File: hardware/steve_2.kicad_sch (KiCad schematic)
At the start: 22 parts, among them J2 Micro_SD_Card_Det2, J3 TE_1-2834015-4_Buchanan_WireM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, U2 TI_TPS51386RJNR_Regulator_Buc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

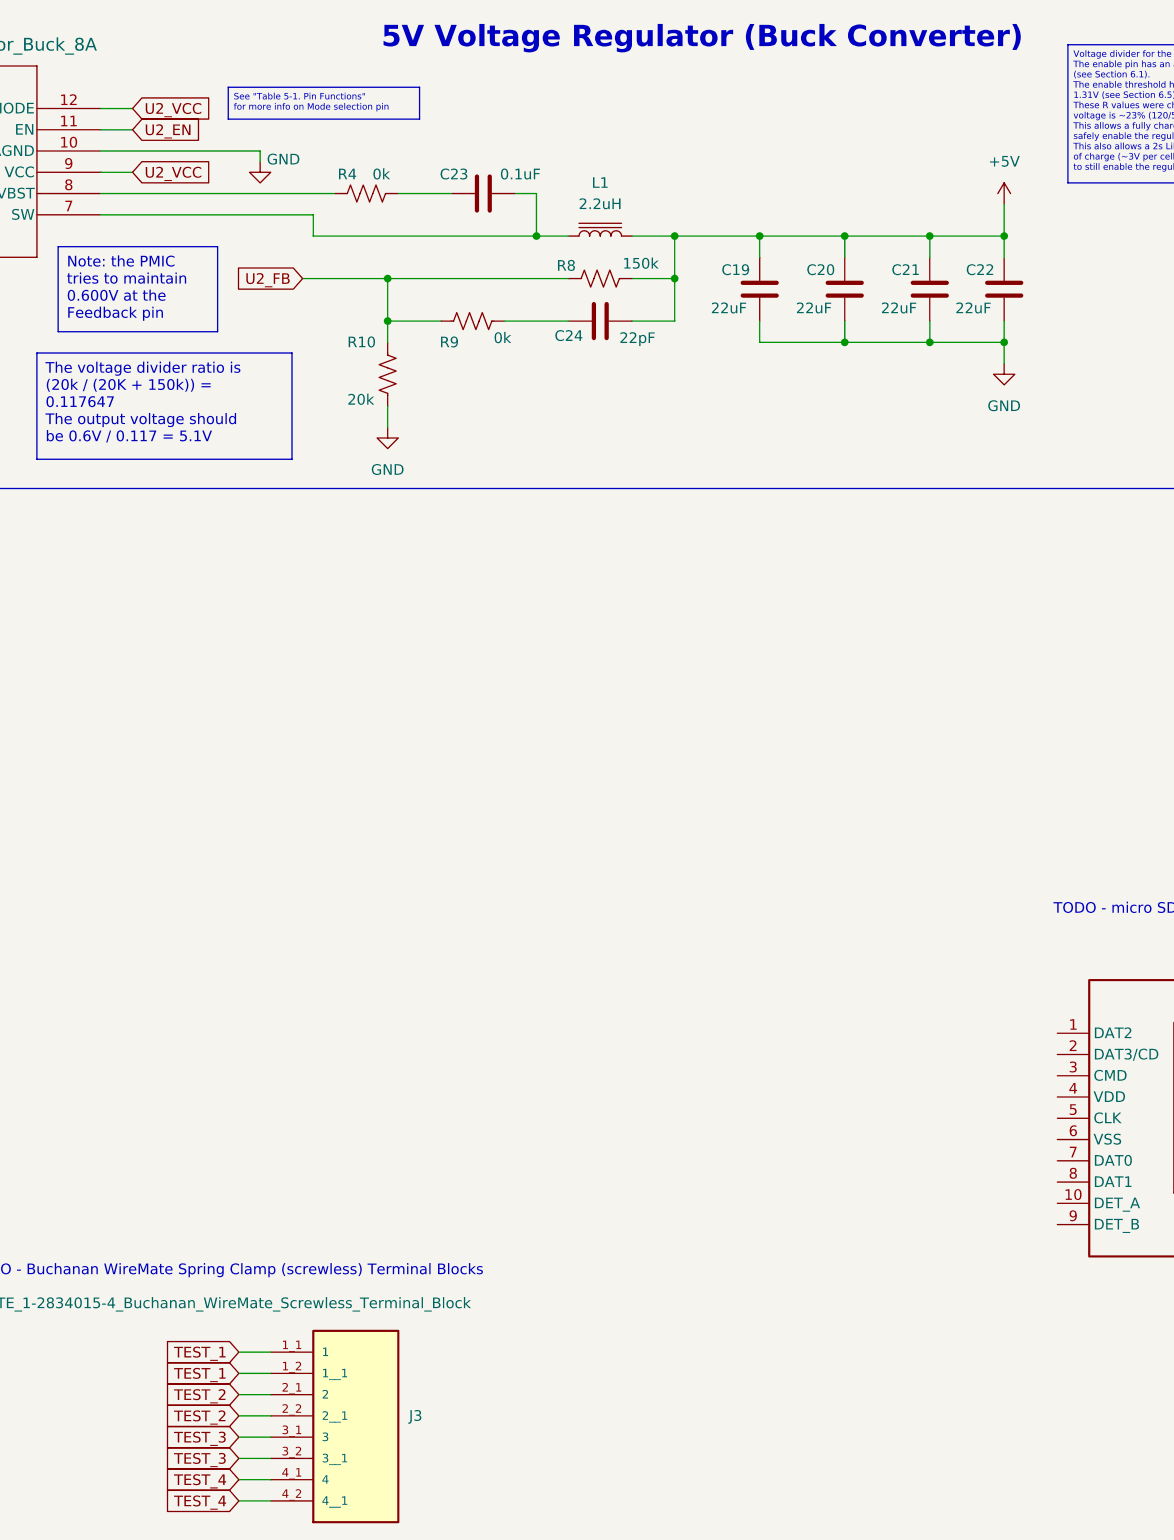
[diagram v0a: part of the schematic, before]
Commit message: import BMP388, add BMP388 to pcb and sch
Import BMP388 symbol and footprint to project imports dir. Add BMP388 symbol to schematic and footprint to pcb.
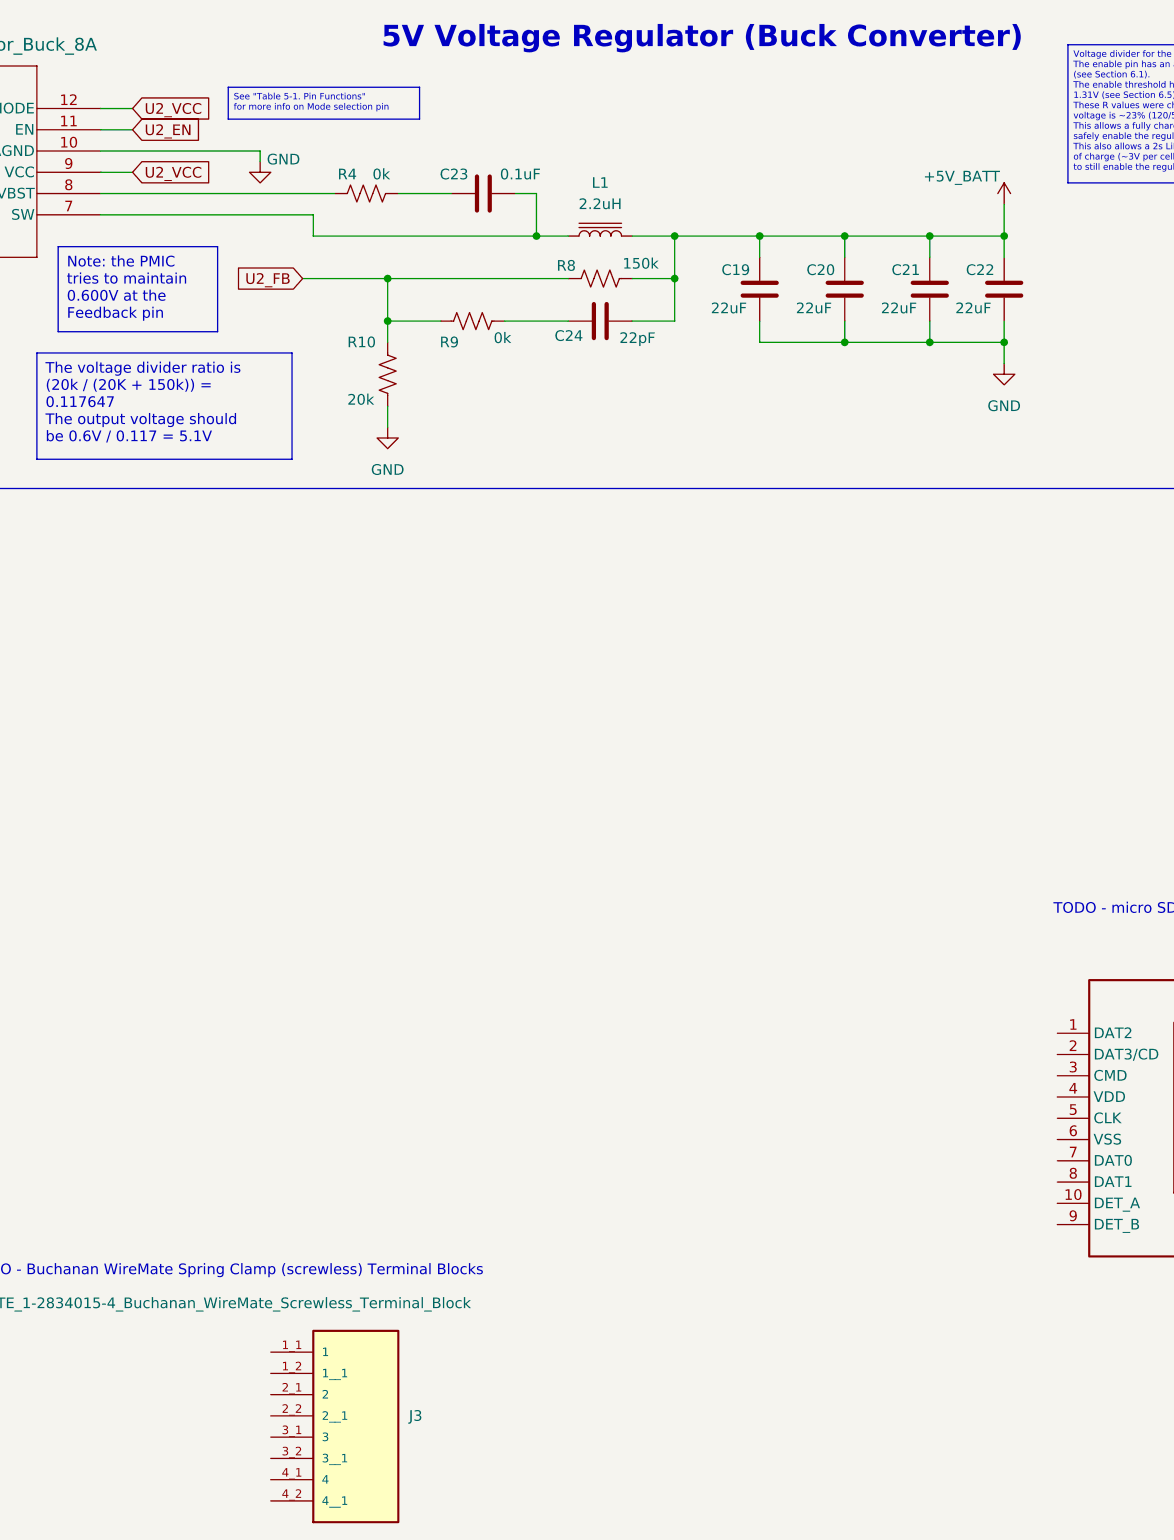
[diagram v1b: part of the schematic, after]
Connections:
- net +5V renamed +5V_BATT
- net TEST_1: no longer names the net of J3.1_1 (1)
- net TEST_1: no longer J3.1_2 (1__1)
- net TEST_2: no longer names the net of J3.2_1 (2)
- net TEST_2: no longer J3.2_2 (2__1)
- net TEST_3: no longer names the net of J3.3_1 (3)
- net TEST_3: no longer J3.3_2 (3__1)
- net TEST_4: no longer names the net of J3.4_1 (4)
- net TEST_4: no longer J3.4_2 (4__1)

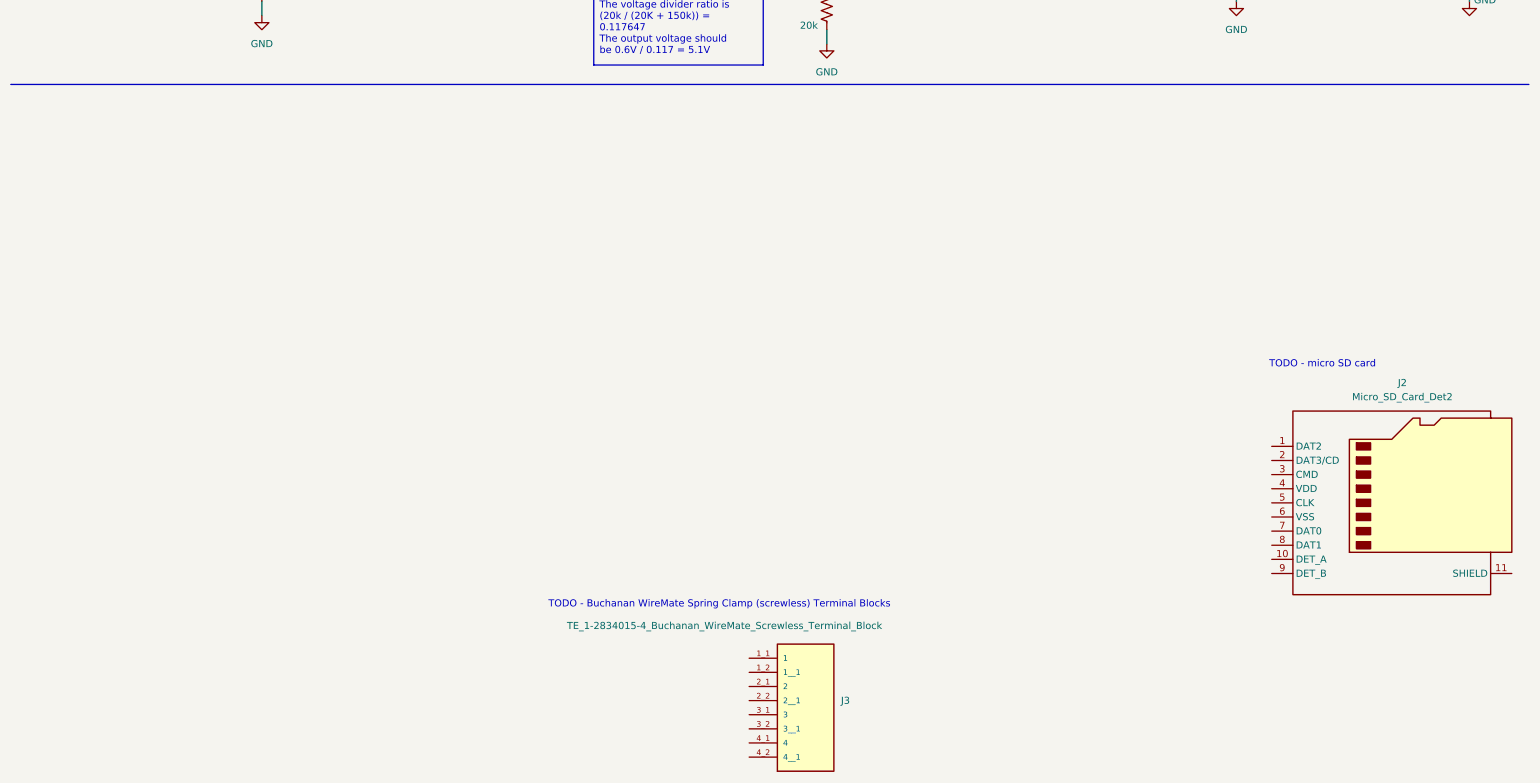
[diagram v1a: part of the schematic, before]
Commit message: Finished sensor, flash, and SD card in schematic; Updated README for remaining items
Finished BMI270 and BMP390, Flash storage, and  microSD card in schematic; Updated README for remaining items
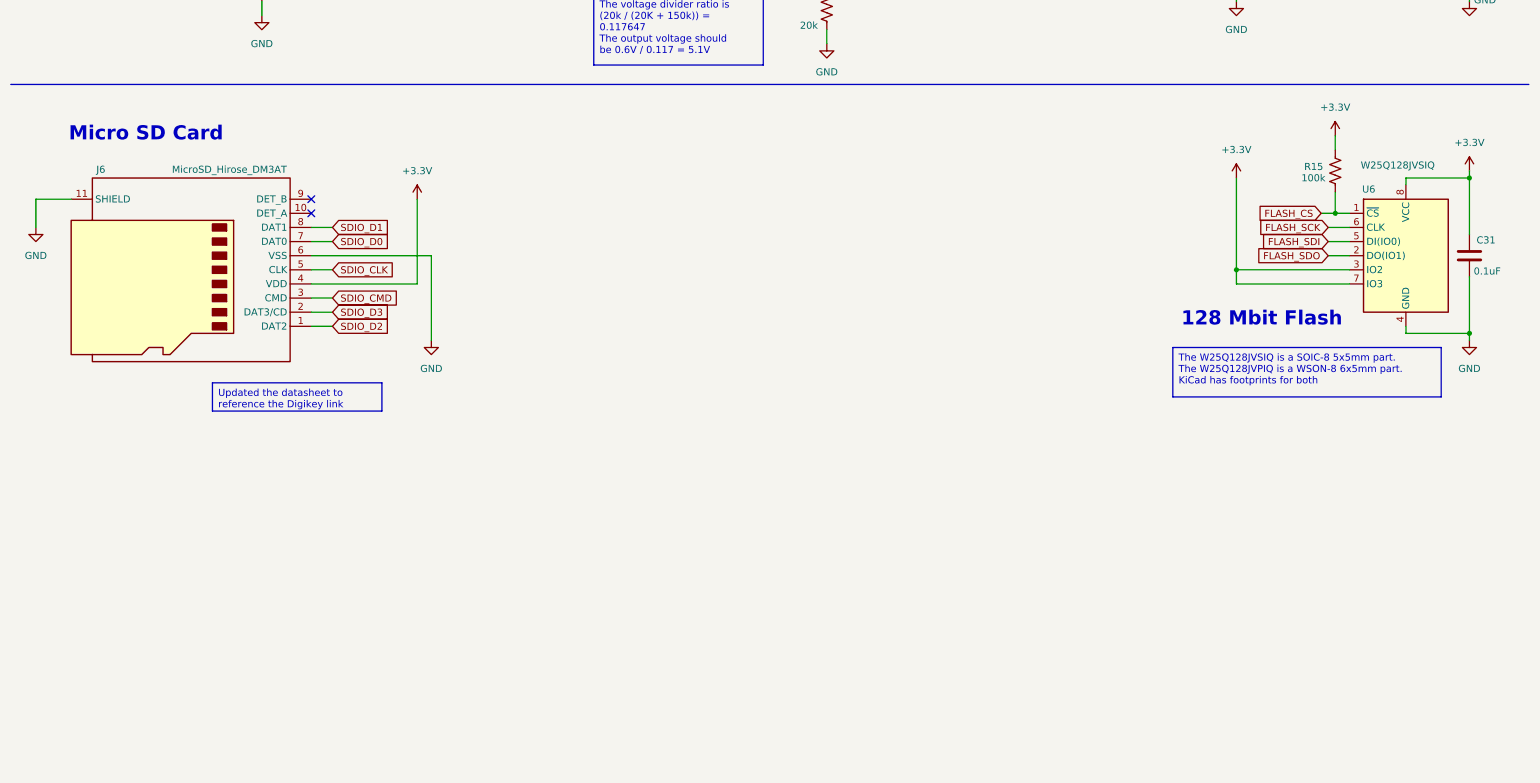
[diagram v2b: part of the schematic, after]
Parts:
- removed J2: Micro_SD_Card_Det2, Connector_Card:microSD_HC_Molex_104031-0811, symbol Connector:Micro_SD_Card_Det2
- removed J3: TE_1-2834015-4_Buchanan_WireMate_Screwless_Termin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, Imported_Footprints:TE_1-2834015-4_Buchanan_WireMate_Screwless_Terminal_Block, symbol Imported_Symbols:TE_1-2834015-4_Buchanan_WireMate_Screwless_Terminal_Block
- added C31: 0.1uF, Capacitor_SMD:C_0603_1608Metric, symbol Device:C
- added J6: MicroSD_Hirose_DM3AT, Connector_Card:microSD_HC_Hirose_DM3AT-SF-PEJM5, symbol Connector:Micro_SD_Card_Det_Hirose_DM3AT
- added R15: 100k, Resistor_SMD:R_0603_1608Metric, symbol Device:R_US
- added U6: W25Q128JVSIQ, Package_SO:SOIC-8_5.23x5.23mm_P1.27mm, symbol Memory_Flash:W25Q128JVS
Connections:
- net GND: now also C31.2, J6.11 (SHIELD), J6.6 (VSS), U6.4 (GND)
- new net +3.3V: C31.1, J6.4 (VDD), R15.1, U6.3 (IO2), U6.7 (IO3), U6.8 (VCC)
- new net FLASH_CS: R15.2, U6.1 (~{CS})
- new net FLASH_SCK: U6.6 (CLK)
- new net FLASH_SDI: U6.5 (DI(IO0))
- new net FLASH_SDO: U6.2 (DO(IO1))
- new net SDIO_CLK: J6.5 (CLK)
- new net SDIO_CMD: J6.3 (CMD)
- new net SDIO_D0: J6.7 (DAT0)
- new net SDIO_D1: J6.8 (DAT1)
- new net SDIO_D2: J6.1 (DAT2)
- new net SDIO_D3: J6.2 (DAT3/CD)
- no-connect marks 1 -> 3
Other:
- note added: "128 Mbit Flash"
- note added: "Micro SD Card"
- note removed: "TODO - Buchanan WireMate Spring Clamp (screwless) Terminal Blocks"
- note removed: "TODO - micro SD card"
